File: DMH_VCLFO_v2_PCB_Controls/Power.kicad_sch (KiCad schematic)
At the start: 17 parts, among them J100 IDC_02x08, J52 Conn_01x06, J53 Conn_01x01, J54 Conn_01x06, U1 TL074, U2 TL074, U3 TL074

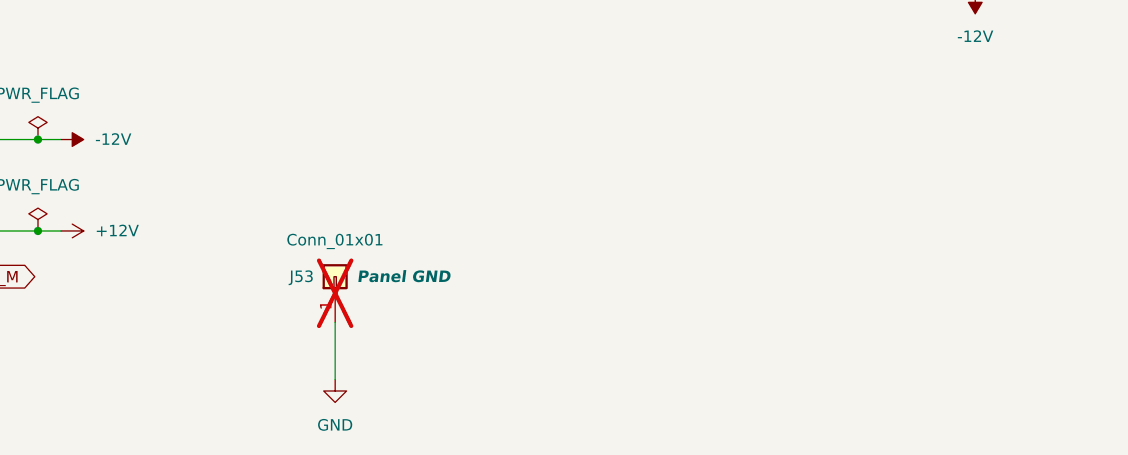
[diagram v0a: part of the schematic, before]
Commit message: Synced Controls PCB with Main
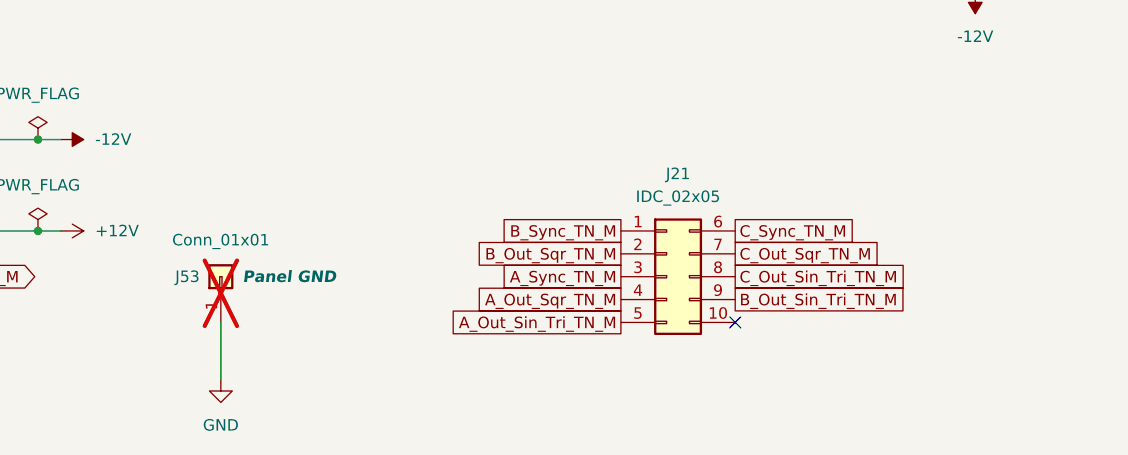
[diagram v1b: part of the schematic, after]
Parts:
- added J21: IDC_02x05, SynthStuff:IDC-Header_2x05_P2.54mm_Vertical_BackBone, symbol SynthStuff:BackBone_Connector_10Pin
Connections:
- new net A_Out_Sin_Tri_TN_M: J21.5 (Pin_5)
- new net A_Out_Sqr_TN_M: J21.4 (Pin_4)
- new net A_Sync_TN_M: J21.3 (Pin_3)
- new net B_Out_Sin_Tri_TN_M: J21.9 (Pin_9)
- new net B_Out_Sqr_TN_M: J21.2 (Pin_2)
- new net B_Sync_TN_M: J21.1 (Pin_1)
- new net C_Out_Sin_Tri_TN_M: J21.8 (Pin_8)
- new net C_Out_Sqr_TN_M: J21.7 (Pin_7)
- new net C_Sync_TN_M: J21.6 (Pin_6)
- no-connect marks 4 -> 5
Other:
- moved on the sheet: J53
